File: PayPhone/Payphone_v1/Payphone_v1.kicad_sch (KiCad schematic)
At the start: 86 parts, among them J1 JST_05, J2 Molex_26-60-4030, J3 Molex_26-60-4040, J6 PINHD_1x5_Male, J7 PINHD_1x2_Male, J8 PINHD_1x2_Male, J9 PINHD_1x2_Male, K1 G6S-2, Q1 2N7002, Q2 MMBT3904, Q3 IRF630, Q4 2N7002, Q5 MMBT3906, U1 MCP23008-xP, U2 MC34063AP, U3 UC3843AN, U4 ADS1115IDGS

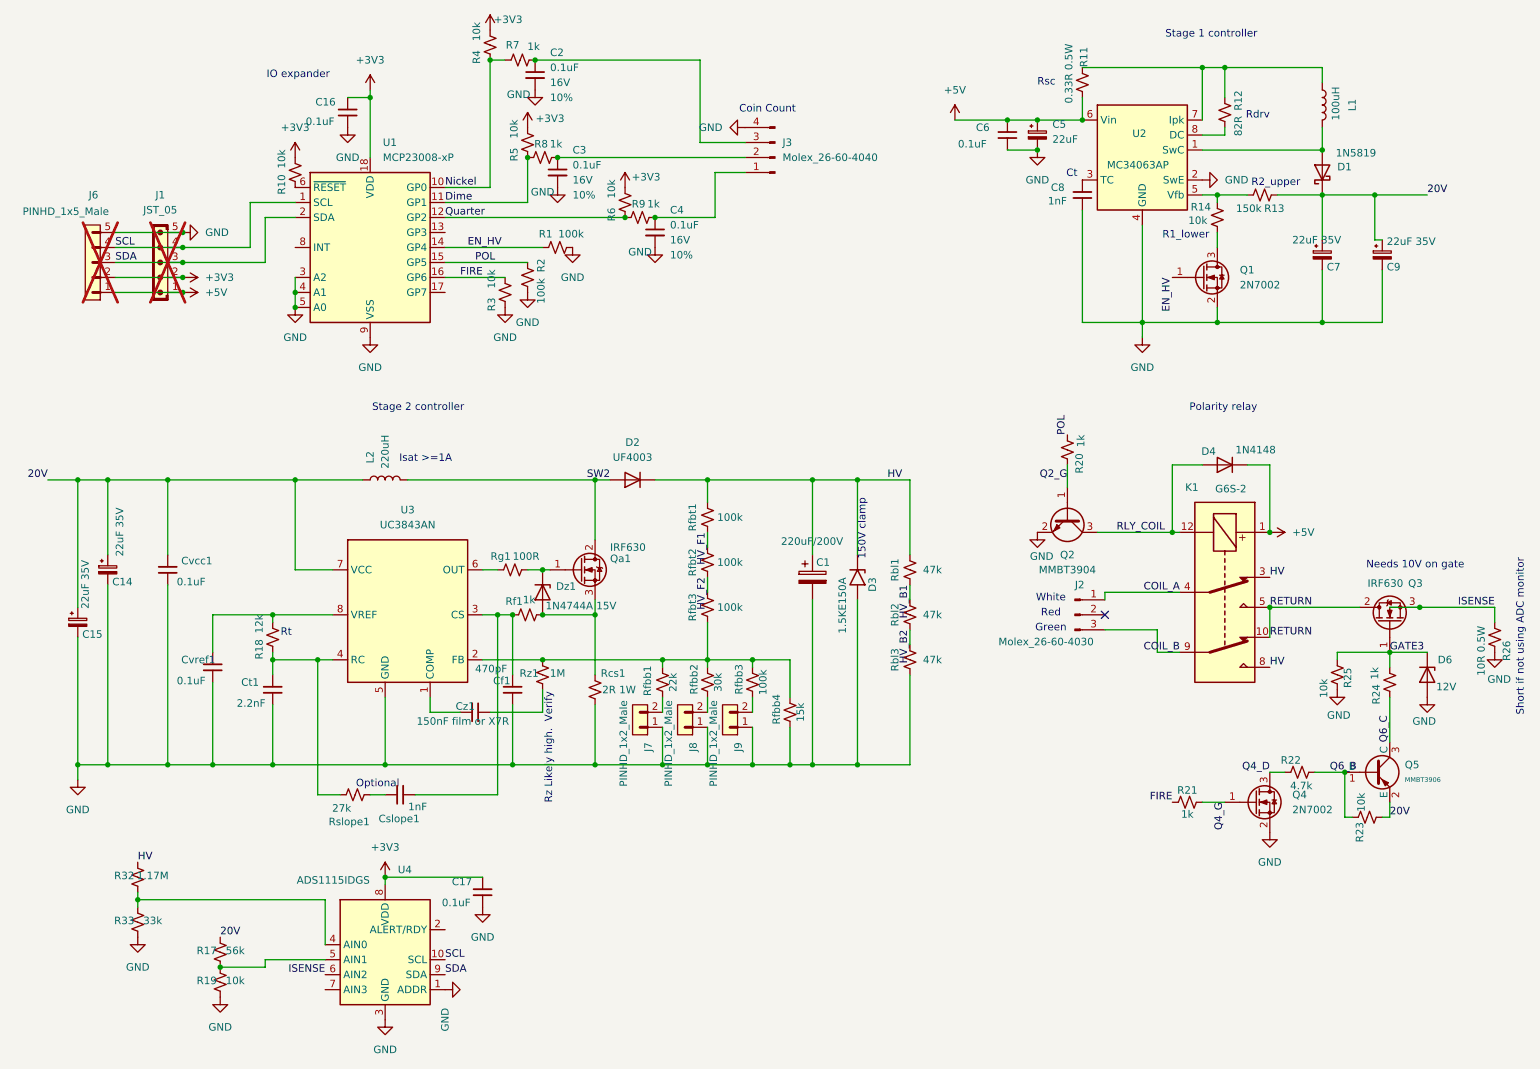
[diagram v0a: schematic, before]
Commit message: Payphone_v1: SMT footprints and part values (U1-U3 SOIC, Q3 STN4NF20L SOT-223, D2/D3/Dz1 SMA/SMB, L1/L2 SRR1260, 22uF SMD electrolytics, 2512/1206 power and HV-chain resistors); C6 connected to +5V; labels match renumbered Q2/Q5; SMT doc: U3 is UC3843BD1R2G, UCC38C43 ruled out (20 V VDD abs max); includes PCB/project edits from the other computer
Co-Authored-By: Claude Opus 5.5 <noreply@anthropic.com>
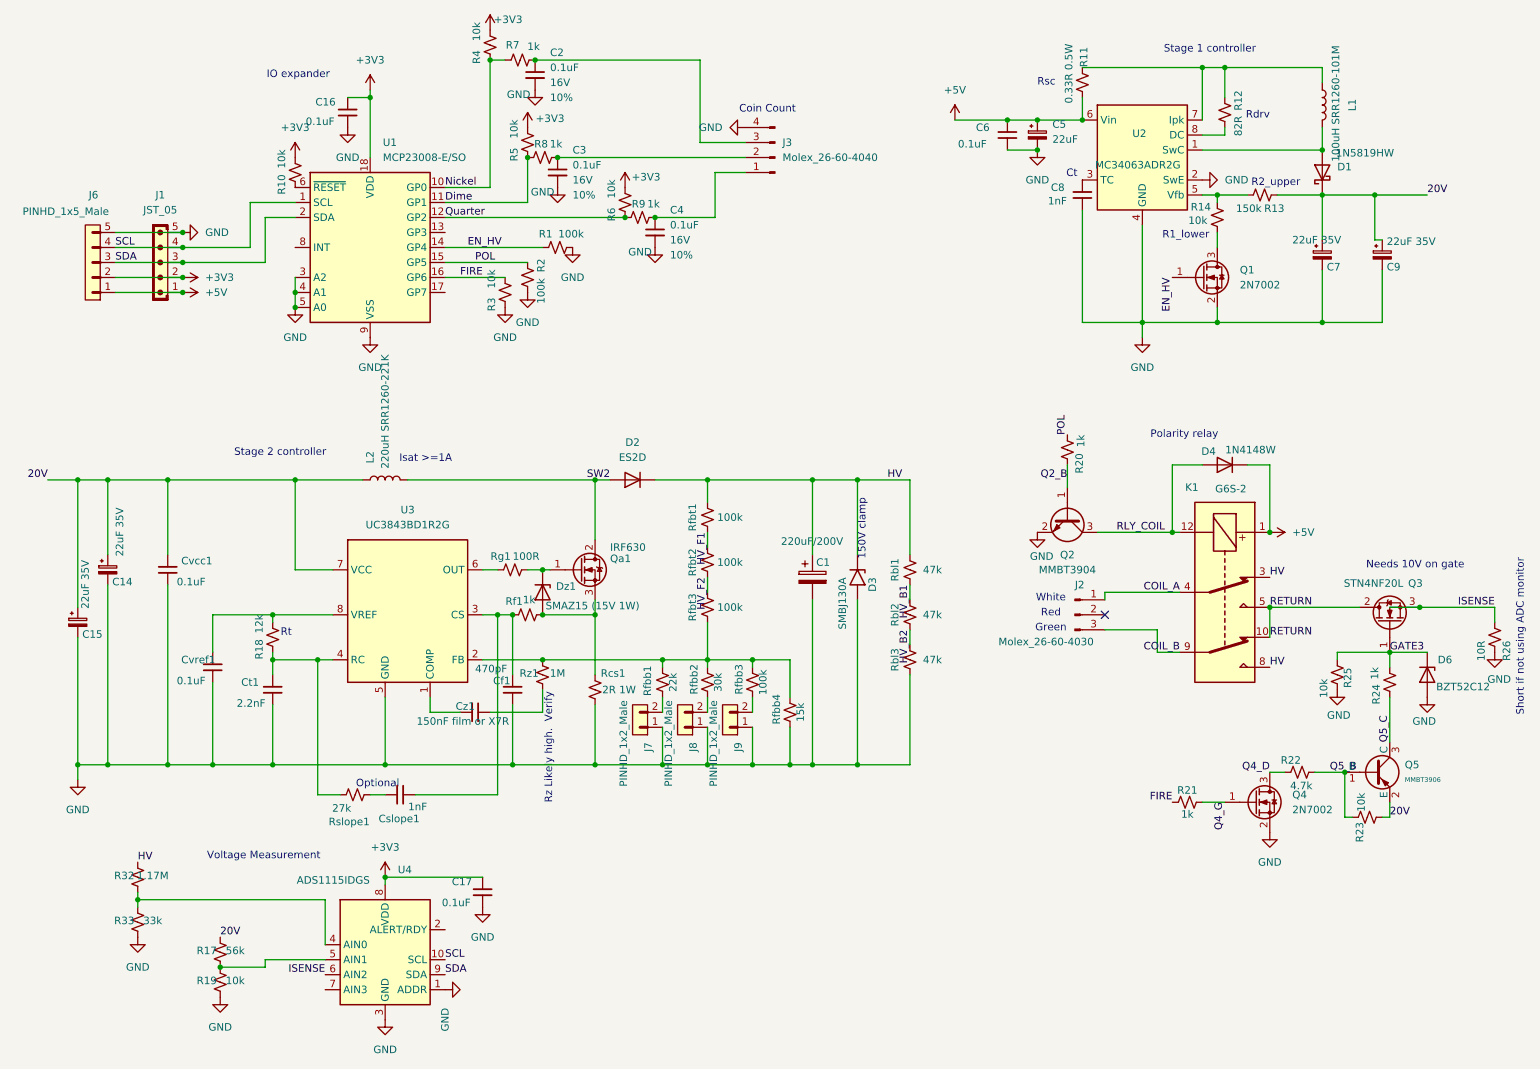
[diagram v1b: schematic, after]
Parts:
- C14, C15, C5, C7, C9: footprint Capacitor_THT:CP_Radial_D5.0mm_P2.00mm -> Capacitor_SMD:CP_Elec_6.3x5.4
- D1: value 1N5819 -> 1N5819HW
- D2: value UF4003 -> ES2D; footprint Diode_THT:D_DO-41_SOD81_P10.16mm_Horizontal -> Diode_SMD:D_SMA
- D3: value 1.5KE150A -> SMBJ130A; footprint Diode_THT:D_DO-201AD_P15.24mm_Horizontal -> Diode_SMD:D_SMB
- D4: value 1N4148 -> 1N4148W
- D6: value 12V -> BZT52C12; footprint Diode_THT:D_DO-41_SOD81_P10.16mm_Horizontal -> Diode_SMD:D_SOD-123
- Dz1: value 1N4744A 15V -> SMAZ15 (15V 1W); footprint Diode_THT:D_DO-41_SOD81_P10.16mm_Horizontal -> Diode_SMD:D_SMA
- J1, J6: now fitted
- L1: value 100uH -> 100uH SRR1260-101M; footprint Inductor_THT:L_Radial_D10.0mm_P5.00mm_Fastron_07M -> Inductor_SMD:L_Bourns_SRR1260
- L2: value 220uH -> 220uH SRR1260-221K; footprint Inductor_THT:L_Radial_D10.0mm_P5.00mm_Fastron_07M -> Inductor_SMD:L_Bourns_SRR1260
- Q3: value IRF630 -> STN4NF20L; footprint Package_TO_SOT_THT:TO-220-3_Vertical -> Package_TO_SOT_SMD:SOT-223-3_TabPin2
- Q5: footprint PCM_JLCPCB:Q_SOT-23 -> Package_TO_SOT_SMD:SOT-23
- R11: footprint Resistor_THT:R_Axial_DIN0309_L9.0mm_D3.2mm_P12.70mm_Horizontal -> Resistor_SMD:R_2512_6332Metric
- R26: value 10R 0.5W -> 10R; footprint Resistor_THT:R_Axial_DIN0309_L9.0mm_D3.2mm_P12.70mm_Horizontal -> Resistor_SMD:R_1206_3216Metric
- R32, Rbl1, Rbl2, Rbl3, Rfbt1, Rfbt2, Rfbt3: footprint Resistor_SMD:R_0805_2012Metric -> Resistor_SMD:R_1206_3216Metric
- Rcs1: footprint Resistor_THT:R_Axial_DIN0414_L11.9mm_D4.5mm_P15.24mm_Horizontal -> Resistor_SMD:R_2512_6332Metric
- U1: value MCP23008-xP -> MCP23008-E/SO; footprint Package_DIP:DIP-18_W7.62mm -> Package_SO:SOIC-18W_7.5x11.6mm_P1.27mm
- U2: value MC34063AP -> MC34063ADR2G; footprint Package_DIP:DIP-8_W7.62mm -> Package_SO:SOIC-8_3.9x4.9mm_P1.27mm
- U3: value UC3843AN -> UC3843BD1R2G; footprint Package_DIP:DIP-8_W7.62mm -> Package_SO:SOIC-8_3.9x4.9mm_P1.27mm
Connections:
- net Q2_G renamed Q2_B
- net Q6_B renamed Q5_B
- net Q6_C renamed Q5_C
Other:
- note added: "Voltage Measurement"
